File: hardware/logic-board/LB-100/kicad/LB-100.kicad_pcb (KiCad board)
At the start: 4 copper layers, 100 x 70 mm, 91 parts, among them U1 STM32H563VIT6, U10 BMI270, U11 VEML7700-TT, U12 TPS22918TDBVRQ1, U13 TPS22918TDBVRQ1, U14 SN74LVC1G17QDBVRQ1, U15 SN74LVC1G125QDBVRQ1, U16 SN74LVC1G125QDBVRQ1, U17 SN74LVC1G125QDBVRQ1, U2 XC6220B331MR-G, U3 TCA9539QPWRQ1, U4 TJA1051TK/3,118, U5 TJA1021T/20/CM,118, U6 SP3485EN-L/TR, U7 E73-2G4M08S1C, U8 FM24CL64B-GTR, U9 DS3231MZ+TRL, Y1 ABM8AIG-25.000MHZ-12-2Z-T3, Y2 ABS07AIG-32.768kHz-7-T

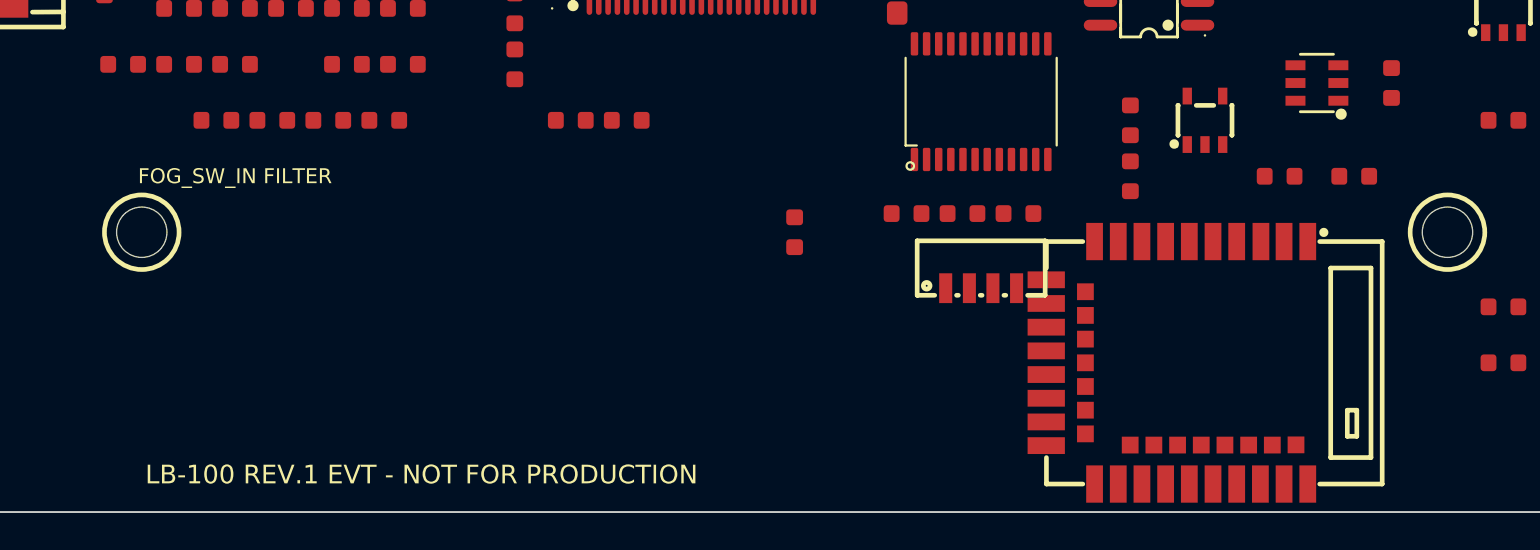
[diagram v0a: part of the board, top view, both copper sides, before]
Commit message: feat: add dual protected fog switch inputs
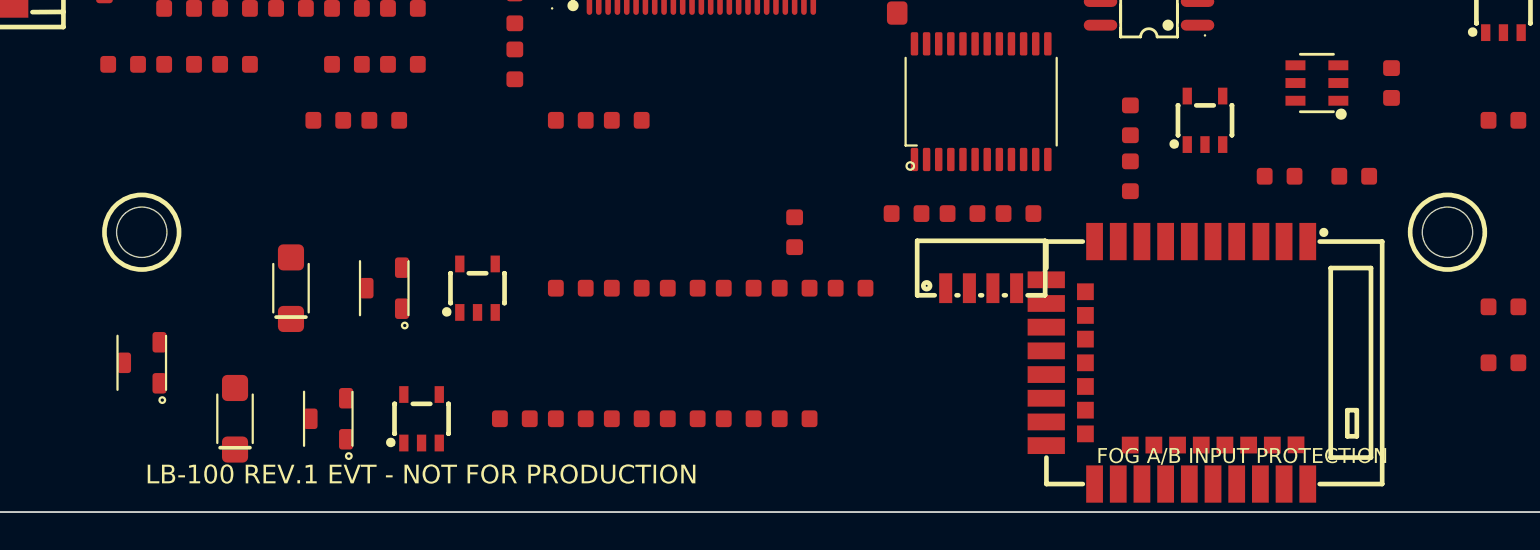
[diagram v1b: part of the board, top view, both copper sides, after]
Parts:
- added C36: 47nF 50V X7R FOG_B filter, LB100:R_C_0603_1608Metric, F.Cu at (35.0, 65.0)
- added C37: 100nF 6.3V X7R U18, LB100:R_C_0603_1608Metric, F.Cu at (41.0, 58.0)
- added C38: 100nF 6.3V X7R U19, LB100:R_C_0603_1608Metric, F.Cu at (38.0, 65.0)
- added D18: ESD2CANFD24DBZRQ1, LB100:SOT-23-3_DBZ_TI, F.Cu at (15.0, 62.0)
- added D19: BZT52H-B4V3-Q, LB100:SOD-123F_L2.6-W1.6, F.Cu at (23.0, 58.0)
- added D20: BZT52H-B4V3-Q, LB100:SOD-123F_L2.6-W1.6, F.Cu at (20.0, 65.0)
- added Q18: BC847BQ-7-F 12V OPTION, LB100:SOT-23-3_DBZ_TI, F.Cu at (28.0, 58.0)
- added Q19: BC847BQ-7-F 12V OPTION, LB100:SOT-23-3_DBZ_TI, F.Cu at (25.0, 65.0)
- added R24: 47k 1% FOG_A 12V base DNP, LB100:R_C_0603_1608Metric, F.Cu at (47.0, 58.0)
- added R25: 100k 1% FOG_A base pull-down DNP, LB100:R_C_0603_1608Metric, F.Cu at (50.0, 58.0)
- added R26: 47k 1% FOG_A pull-up, LB100:R_C_0603_1608Metric, F.Cu at (53.0, 58.0)
- added R27: 4.7k 1% FOG_B dry-contact series, LB100:R_C_0603_1608Metric, F.Cu at (41.0, 65.0)
- added R28: 47k 1% FOG_B 12V base DNP, LB100:R_C_0603_1608Metric, F.Cu at (44.0, 65.0)
- added R29: 100k 1% FOG_B base pull-down DNP, LB100:R_C_0603_1608Metric, F.Cu at (47.0, 65.0)
- added R30: 47k 1% FOG_B pull-up, LB100:R_C_0603_1608Metric, F.Cu at (50.0, 65.0)
- added U18: SN74LVC1G17QDBVRQ1, LB100:SOT-25_L3.0-W1.6-P0.95-LS2.8-TL, F.Cu at (33.0, 58.0)
- added U19: SN74LVC1G17QDBVRQ1, LB100:SOT-25_L3.0-W1.6-P0.95-LS2.8-TL, F.Cu at (30.0, 65.0)
- C35: value 10nF 50V X7R fog input filter -> 47nF 50V X7R FOG_A filter
- R23: value 10k 1% fog input pull-up -> 4.7k 1% FOG_A dry-contact series
- moved R23 23.8 mm to (44.0, 58.0)
- moved C35 21.0 mm to (38.0, 58.0)
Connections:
- C35 pad 1: FOG_SW_IN -> FOG_A_FILTERED
- JPB1 pad 82: FOG_SW_IN -> FOG_A_SW_IN
- JPB1 pad 83: EXT_DIG2 -> FOG_B_SW_IN
- R23 pad 1: LB_3V3_IO -> FOG_A_SW_IN
- R23 pad 2: FOG_SW_IN -> FOG_A_FILTERED
- U1 pad 67: FOG_SW_IN -> FOG_A_SW_IN_MCU
- U1 pad 68: EXT_DIG2 -> FOG_B_SW_IN_MCU
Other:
- board text added: "FOG A/B INPUT PROTECTION"
- board text removed: "FOG_SW_IN FILTER"

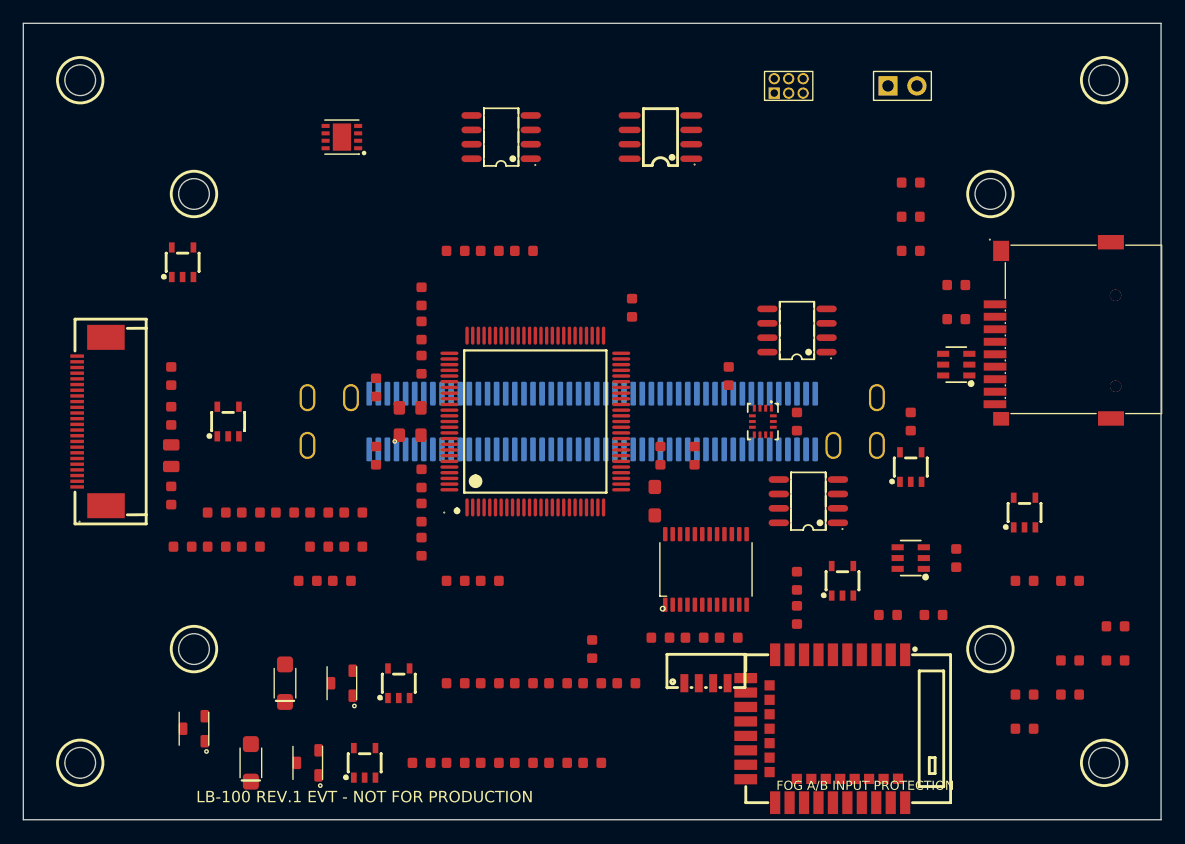
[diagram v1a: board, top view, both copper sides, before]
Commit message: feat(hardware): add EVT board routing milestones
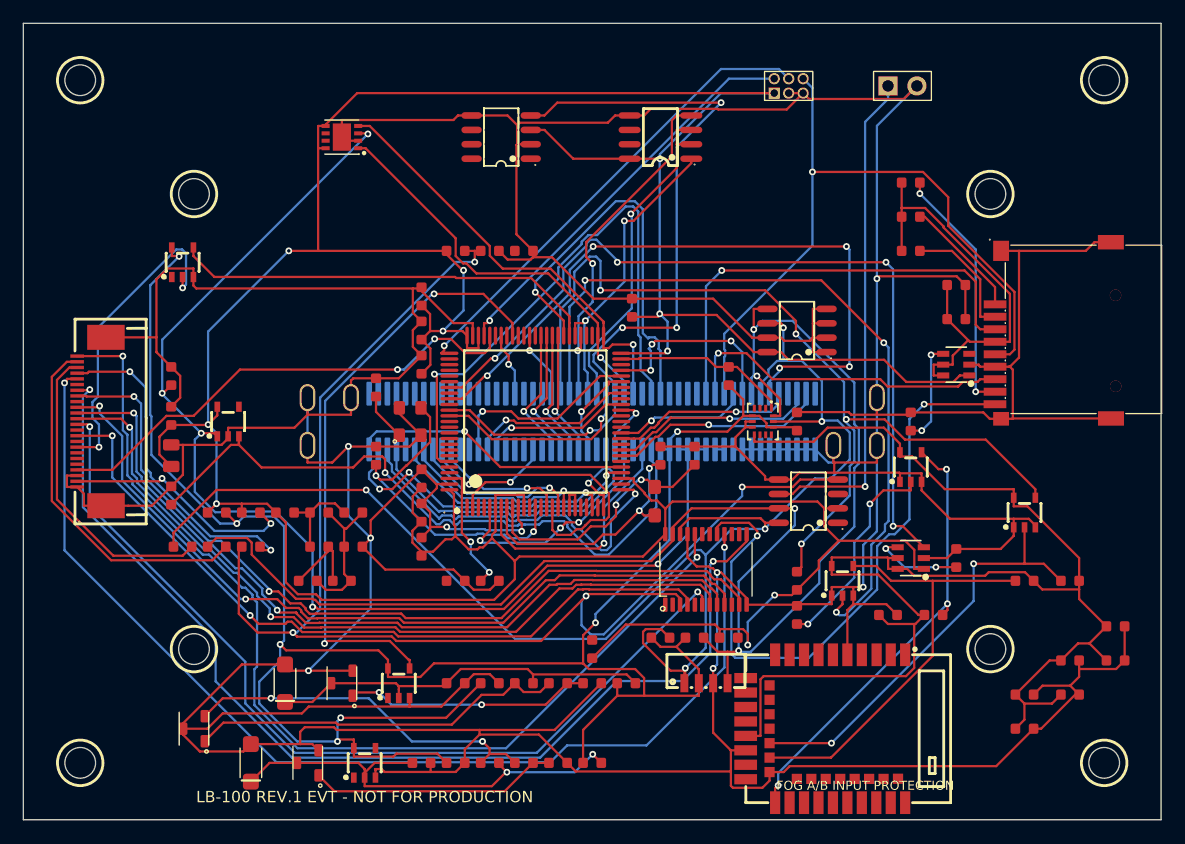
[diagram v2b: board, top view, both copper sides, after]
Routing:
- net GND: track 0.00 -> 729.0 mm, vias 0 -> 9
- net LB_3V3_MAIN: track 0.00 -> 350.4 mm, vias 0 -> 10
- net LB_3V3_IO: track 0.00 -> 188.7 mm, vias 0 -> 7
- net PB_I2C_SDA: track 0.00 -> 134.3 mm, vias 0 -> 4
- net PB_I2C_SCL: track 0.00 -> 131.7 mm, vias 0 -> 5
- net RADIO_SENSOR_3V3: track 0.00 -> 127.2 mm
- net NRST: track 0.00 -> 122.7 mm, vias 0 -> 4
- net PB_5V_OUT: track 0.00 -> 107.4 mm, vias 0 -> 5
- net SERVICE_BTN: track 0.00 -> 96.9 mm, vias 0 -> 2
- net CH_LED_9: track 0.00 -> 94.4 mm, vias 0 -> 2
- net OLED_RST_OR_INT_DNP: track 0.00 -> 89.7 mm, vias 0 -> 2
- net UART_RX: track 0.00 -> 81.5 mm, vias 0 -> 4
- net CH_LED_3: track 0.00 -> 79.9 mm, vias 0 -> 2
- net CH_LED_8: track 0.00 -> 73.5 mm, vias 0 -> 2
- net RADIO_SENSOR_EN: track 0.00 -> 72.8 mm, vias 0 -> 4
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
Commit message: hardware: correct fog entry and EVT layout gates
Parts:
- removed D18: ESD2CANFD24DBZRQ1, LB100:SOT-23-3_DBZ_TI
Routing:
- net FOG_B_SW_IN: track 31.6 -> 92.7 mm, vias 2 -> 4
- net FOG_A_SW_IN: track 33.2 -> 72.9 mm, vias 0 -> 2
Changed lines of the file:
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@@
 		(embedded_fonts no)
 	)
-	(footprint "LB100:SOT-23-3_DBZ_TI"
-	  (version 20260206)
-	  (generator "codex")
-	  (layer "F.Cu")
-		(at 15.00 62.00 90)
-	  (descr "TI DBZ / SOT-23-3 automotive protection and transistor package")
-	  (property "Reference" "D18" (at 0 -2.5 0) (layer "F.SilkS")
-			(hide yes) (effects (font (size 0.8 0.8) (thickness 0.12))))
-	  (property "Value" "ESD2CANFD24DBZRQ1" (at 0 2.5 0) (layer "F.Fab") (effects (font (size 0.8 0.8) (thickness 0.12))))
-	  (attr smd)
-	  (fp_rect (start -1.45 -1.15) (end 1.45 1.15) (stroke (width 0.1) (type default)) (fill none) (layer "F.Fab"))
-	  (fp_line (start -1.45 -1.3) (end 1.45 -1.3) (stroke (width 0.12) (type default)) (layer "F.SilkS"))
-	  (fp_line (start -1.45 1.3) (end 1.45 1.3) (stroke (width 0.12) (type default)) (layer "F.SilkS"))
-	  (fp_circle (center -2 1.1) (end -1.85 1.1) (stroke (width 0.12) (type default)) (fill none) (layer "F.SilkS"))
-	  (fp_rect (start -2.5 -1.6) (end 2.5 1.6) (stroke (width 0.05) (type default)) (fill none) (layer "F.CrtYd"))
-	  (pad "1" smd roundrect (at -1.1 0.95 90) (size 1.1 0.75) (layers "F.Cu" "F.Paste" "F.Mask") (roundrect_rratio 0.2)
-			(net 31 "FOG_A_SW_IN")
-			(pinfunction "IO1")
-			(pintype "passive")
-		)
-	  (pad "2" smd roundrect (at 1.1 0.95 90) (size 1.1 0.75) (layers "F.Cu" "F.Paste" "F.Mask") (roundrect_rratio 0.2)
-			(net 35 "FOG_B_SW_IN")
-			(pinfunction "IO2")
-			(pintype "passive")
-		)
-	  (pad "3" smd roundrect (at 0 -0.95 90) (size 1.1 0.75) (layers "F.Cu" "F.Paste" "F.Mask") (roundrect_rratio 0.2)
-			(net 37 "GND")
-			(pinfunction "GND")
-			(pintype "power_in")
-		)
-		(property "Datasheet" "https://www.ti.com/lit/ds/symlink/esd2can24-q1.pdf" (at 0 0 0) (layer "F.Fab") (hide yes) (effects (font (size 1.27 1.27))))
-	)
 	(footprint "LB100:SOD-123F_L2.6-W1.6"
 	  (version 20260206)
@@
 	(segment (start 44.800000 58.000000) (end 44.800000 57.227300) (width 0.200000) (layer "F.Cu") (net 30))
 	(segment (start 53.027300 57.227300) (end 53.800000 58.000000) (width 0.200000) (layer "F.Cu") (net 30))
-	(segment (start 17.584500 61.465500) (end 15.950000 63.100000) (width 0.200000) (layer "F.Cu") (net 31))
 	(segment (start 27.473300 61.465500) (end 17.584500 61.465500) (width 0.200000) (layer "F.Cu") (net 31))
 	(segment (start 27.648400 61.640600) (end 27.473300 61.465500) (width 0.200000) (layer "F.Cu") (net 31))
@@
 	(segment (start 30.357000 59.323100) (end 34.150200 63.116300) (width 0.200000) (layer "B.Cu") (net 35))
 	(segment (start 34.150200 63.116300) (end 40.362200 63.116300) (width 0.200000) (layer "B.Cu") (net 35))
-	(segment (start 15.950000 60.900000) (end 17.526900 59.323100) (width 0.200000) (layer "F.Cu") (net 35))
 	(segment (start 17.526900 59.323100) (end 21.769000 59.323100) (width 0.200000) (layer "F.Cu") (net 35))
 	(segment (start 40.980200 63.734300) (end 40.362200 63.116300) (width 0.200000) (layer "F.Cu") (net 35))
@@
 	(via (at 21.769000 59.323100) (size 0.600000) (drill 0.300000) (layers "F.Cu" "B.Cu") (net 35))
 	(via (at 40.362200 63.116300) (size 0.600000) (drill 0.300000) (layers "F.Cu" "B.Cu") (net 35))
+	(via (at 17.584500 61.465500) (size 0.600000) (drill 0.300000) (layers "F.Cu" "In1.Cu") (net 31))
+	(segment (start 17.584500 61.465500) (end 44.800000 31.200000) (width 0.200000) (layer "In1.Cu") (net 31))
+	(via (at 44.800000 31.200000) (size 0.600000) (drill 0.300000) (layers "In1.Cu" "B.Cu") (net 31))
+	(segment (start 44.800000 31.200000) (end 44.800000 32.550000) (width 0.200000) (layer "B.Cu") (net 31))
+	(via (at 17.526900 59.323100) (size 0.600000) (drill 0.300000) (layers "F.Cu" "In2.Cu") (net 35))
+	(segment (start 17.526900 59.323100) (end 18.000000 56.000000) (width 0.200000) (layer "In2.Cu") (net 35))
+	(segment (start 18.000000 56.000000) (end 18.000000 50.000000) (width 0.200000) (layer "In2.Cu") (net 35))
+	(segment (start 18.000000 50.000000) (end 18.000000 40.000000) (width 0.200000) (layer "In2.Cu") (net 35))
+	(segment (start 18.000000 40.000000) (end 18.000000 29.000000) (width 0.200000) (layer "In2.Cu") (net 35))
+	(segment (start 18.000000 29.000000) (end 35.000000 29.000000) (width 0.200000) (layer "In2.Cu") (net 35))
+	(segment (start 35.000000 29.000000) (end 35.000000 33.000000) (width 0.200000) (layer "In2.Cu") (net 35))
+	(segment (start 35.000000 33.000000) (end 40.000000 33.000000) (width 0.200000) (layer "In2.Cu") (net 35))
+	(segment (start 40.000000 33.000000) (end 44.000000 30.400000) (width 0.200000) (layer "In2.Cu") (net 35))
+	(via (at 44.000000 30.400000) (size 0.600000) (drill 0.300000) (layers "In2.Cu" "B.Cu") (net 35))
+	(segment (start 44.000000 30.400000) (end 44.000000 32.550000) (width 0.200000) (layer "B.Cu") (net 35))
 	(via (at 25.062500 56.900000) (size 0.600000) (drill 0.300000) (layers "F.Cu" "B.Cu") (net 37))
 	(via (at 28.571000 37.182400) (size 0.600000) (drill 0.300000) (layers "F.Cu" "B.Cu") (net 37))

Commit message: feat: add E73 recovery and persistent CAN logging
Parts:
- added TP1: E73_SWDIO, LB100:TestPoint_SMD_1.2mm, F.Cu at (98.0, 46.5)
- added TP2: E73_SWDCLK, LB100:TestPoint_SMD_1.2mm, F.Cu at (98.0, 36.5)
- added TP3: BLE_RESET_N, LB100:TestPoint_SMD_1.2mm, F.Cu at (98.0, 39.0)
- added TP4: RADIO_SENSOR_3V3, LB100:TestPoint_SMD_1.2mm, F.Cu at (98.0, 41.5)
- added TP5: GND, LB100:TestPoint_SMD_1.2mm, F.Cu at (98.0, 44.0)
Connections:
- U7 pad 37: (no net) -> E73_SWDIO
- U7 pad 39: (no net) -> E73_SWDCLK
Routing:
- net E73_SWDCLK: track 0.00 -> 42.2 mm, vias 0 -> 2
- net E73_SWDIO: track 0.00 -> 32.8 mm, vias 0 -> 2
- net BLE_RESET_N: track 39.6 -> 56.4 mm, vias 3 -> 4
- net RADIO_SENSOR_3V3: track 127.2 -> 136.3 mm, vias 0 -> 2
- net GND: track 729.0 -> 738.1 mm, vias 9 -> 11

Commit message: feat: harden LB RF layout and CAN logging
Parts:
- moved R21 13.9 mm to (61.0, 64.0), turned to 0 degrees
- moved R9 11.2 mm to (82.0, 63.0)
- moved C32 4.00 mm to (80.0, 52.0)
- moved U7 3.35 mm to (72.0, 59.0), turned to 0 degrees
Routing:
- net GND: track 738.1 -> 682.7 mm, vias 11 -> 10
- net BLE_RESET_N: track 56.4 -> 105.3 mm
- net RADIO_SENSOR_3V3: track 136.3 -> 181.2 mm, vias 2 -> 4
- net E73_SWDIO: track 32.8 -> 62.2 mm
- net UART_TX: track 67.3 -> 89.1 mm
- net BLE_RESET_N_MCU: track 18.6 -> 37.9 mm
- net MICROSD_CARD_DETECT: track 56.3 -> 37.1 mm
- net E73_SWDCLK: track 42.2 -> 60.9 mm
- net BLE_UART_TX_MODULE: track 37.9 -> 29.2 mm
- net BLE_UART_RX_MODULE: track 39.4 -> 32.5 mm, vias 0 -> 2
- net PB_I2C_SDA: track 134.3 -> 131.4 mm
- net LB_3V3_MAIN: track 350.4 -> 353.2 mm
- net PB_PWR_GOOD: track 59.8 -> 59.0 mm
- added copper zone on B.Cu, net GND
- added copper zone on F.Cu, net GND
- added copper zone on In1.Cu, net GND
- added copper zone on In2.Cu, net GND
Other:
- board text added: "E73 ANTENNA - ALL-COPPER KEEPOUT"
- board text removed: "BLE ANTENNA - COPPER KEEPOUT REVIEW"
